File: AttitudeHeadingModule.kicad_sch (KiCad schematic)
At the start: 8 parts, among them J2 Conn_01x04, U2 ISM330DHCX, U3 MMC5983MA

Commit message: Add footprints to symbols
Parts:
- C13, C14, C17: footprint (none) -> Capacitor_SMD:C_0402_1005Metric; Listing (none) -> https://www.digikey.com/en/products/detail/samsung-electro-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
- C15: footprint (none) -> Capacitor_SMD:C_0603_1608Metric; Listing (none) -> https://www.digikey.com/en/products/detail/samsung-electro-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
- C16: footprint (none) -> Capacitor_SMD:C_1206_3216Metric; Listing (none) -> https://www.digikey.com/en/products/detail/samsung-electro-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
- J2: footprint Connector_JST_GH:GH_B04B-GH-A_1x04_P1.25mm_Vertical -> Connector_JST:JST_GH_BM04B-GHS-TBT_1x04-1MP_P1.25mm_Vertical; Listing (none) -> https://www.digikey.com/en/products/detail/jst-sales-americ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
- U2: Listing (none) -> https://www.digikey.com/en/products/detail/stmicroelectroni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
- U3: footprint MMC5983MA_MEM -> XuLab:MMC5983MA_MEM; Listing (none) -> https://www.digikey.com/en/products/detail/memsic-inc/MMC59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
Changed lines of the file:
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@@
 			)
 		)
-		(property "Footprint" "Connector_JST_GH:GH_B04B-GH-A_1x04_P1.25mm_Vertical"
+		(property "Footprint" "Connector_JST:JST_GH_BM04B-GHS-TBT_1x04-1MP_P1.25mm_Vertical"
 			(at 231.394 74.93 0)
 			(effects
@@
 			)
 		)
+		(property "Listing" "https://www.digikey.com/en/products/detail/jst-sales-america-inc/BM04B-GHS-TBT-LF-SN-N/807802"
+			(at 228.6 86.36 0)
+			(effects
+				(font
+					(size 1.27 1.27)
+				)
+				(hide yes)
+			)
+		)
 		(pin "2"
 		)
@@
 			)
 		)
-		(property "Footprint" ""
+		(property "Footprint" "Capacitor_SMD:C_0603_1608Metric"
 			(at 140.6652 123.19 0)
 			(effects
@@
 			)
 		)
-		(property "Datasheet" "~"
+		(property "Datasheet" "https://weblib.samsungsem.com/mlcc/mlcc-ec-data-sheet.do?partNumber=CL10B105KO8NNN"
 			(at 139.7 119.38 0)
 			(effects
@@
 			)
 		)
+		(property "Listing" "https://www.digikey.com/en/products/detail/samsung-electro-mechanics/CL10B105KO8NNNC/3886677"
+			(at 139.7 119.38 0)
+			(effects
+				(font
+					(size 1.27 1.27)
+				)
+				(hide yes)
+			)
+		)
 		(pin "1"
 		)
@@
 			)
 		)
-		(property "Footprint" "MMC5983MA_MEM"
+		(property "Footprint" "XuLab:MMC5983MA_MEM"
 			(at 60.96 134.874 0)
 			(effects
@@
 		)
 		(property "Description" ""
+			(at 81.28 116.84 0)
+			(effects
+				(font
+					(size 1.27 1.27)
+				)
+				(hide yes)
+			)
+		)
+		(property "Listing" "https://www.digikey.com/en/products/detail/memsic-inc/MMC5983MA/10452795"
 			(at 81.28 116.84 0)
 			(effects
@@
 			)
 		)
-		(property "Footprint" ""
+		(property "Footprint" "Capacitor_SMD:C_0402_1005Metric"
 			(at 121.6152 55.88 0)
 			(effects
@@
 			)
 		)
-		(property "Datasheet" "~"
+		(property "Datasheet" "https://mm.digikey.com/Volume0/opasdata/d220001/medias/docus/503/CL05A104KA5NNNC.pdf"
 			(at 120.65 52.07 0)
 			(effects
@@
 			)
 		)
+		(property "Listing" "https://www.digikey.com/en/products/detail/samsung-electro-mechanics/CL05A104KA5NNNC/3886701"
+			(at 120.65 52.07 0)
+			(effects
+				(font
+					(size 1.27 1.27)
+				)
+				(hide yes)
+			)
+		)
 		(pin "1"
 		)
@@
 			)
 		)
+		(property "Listing" "https://www.digikey.com/en/products/detail/stmicroelectronics/ISM330DHCXTR/10409727?s=N4IgTCBcDaIJIGUCyBmFAGAIgCQMIA0QBdAXyA"
+			(at 81.28 53.34 0)
+			(effects
+				(font
+					(size 1.27 1.27)
+				)
+				(hide yes)
+			)
+		)
 		(pin "5"
 		)
@@
 			)
 		)
-		(property "Footprint" ""
+		(property "Footprint" "Capacitor_SMD:C_0402_1005Metric"
 			(at 254.9652 92.71 0)
 			(effects
@@
 			)
 		)
-		(property "Datasheet" "~"
+		(property "Datasheet" "https://mm.digikey.com/Volume0/opasdata/d220001/medias/docus/503/CL05A104KA5NNNC.pdf"
 			(at 254 88.9 0)
 			(effects
@@
 			)
 		)
+		(property "Listing" "https://www.digikey.com/en/products/detail/samsung-electro-mechanics/CL05A104KA5NNNC/3886701"
+			(at 254 88.9 0)
+			(effects
+				(font
+					(size 1.27 1.27)
+				)
+				(hide yes)
+			)
+		)
 		(pin "1"
 		)
@@
 			)
 		)
-		(property "Footprint" ""
+		(property "Footprint" "Capacitor_SMD:C_1206_3216Metric"
 			(at 122.8852 130.81 0)
 			(effects
@@
 			)
 		)
-		(property "Datasheet" "~"
+		(property "Datasheet" "https://mm.digikey.com/Volume0/opasdata/d220001/medias/docus/658/CL31B106KAHNNNE_Spec.pdf"
 			(at 121.92 127 0)
 			(effects
@@
 			)
 		)
+		(property "Listing" "https://www.digikey.com/en/products/detail/samsung-electro-mechanics/CL31B106KAHNNNE/3887462"
+			(at 121.92 127 0)
+			(effects
+				(font
+					(size 1.27 1.27)
+				)
+				(hide yes)
+			)
+		)
 		(pin "1"
 		)
@@
 			)
 		)
-		(property "Footprint" ""
+		(property "Footprint" "Capacitor_SMD:C_0402_1005Metric"
 			(at 134.3152 55.88 0)
 			(effects
@@
 			)
 		)
-		(property "Datasheet" "~"
+		(property "Datasheet" "https://mm.digikey.com/Volume0/opasdata/d220001/medias/docus/503/CL05A104KA5NNNC.pdf"
 			(at 133.35 52.07 0)
 			(effects
@@
 			(at 133.35 52.07 0)
 			(effects
+				(font
+					(size 1.27 1.27)
+				)
+				(hide yes)
+			)
+		)
+		(property "Listing" "https://www.digikey.com/en/products/detail/samsung-electro-mechanics/CL05A104KA5NNNC/3886701"
+			(at 133.35 52.07 0)
+			(effects

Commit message: Add rest of connections
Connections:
- net +3V3 renamed +3.3V

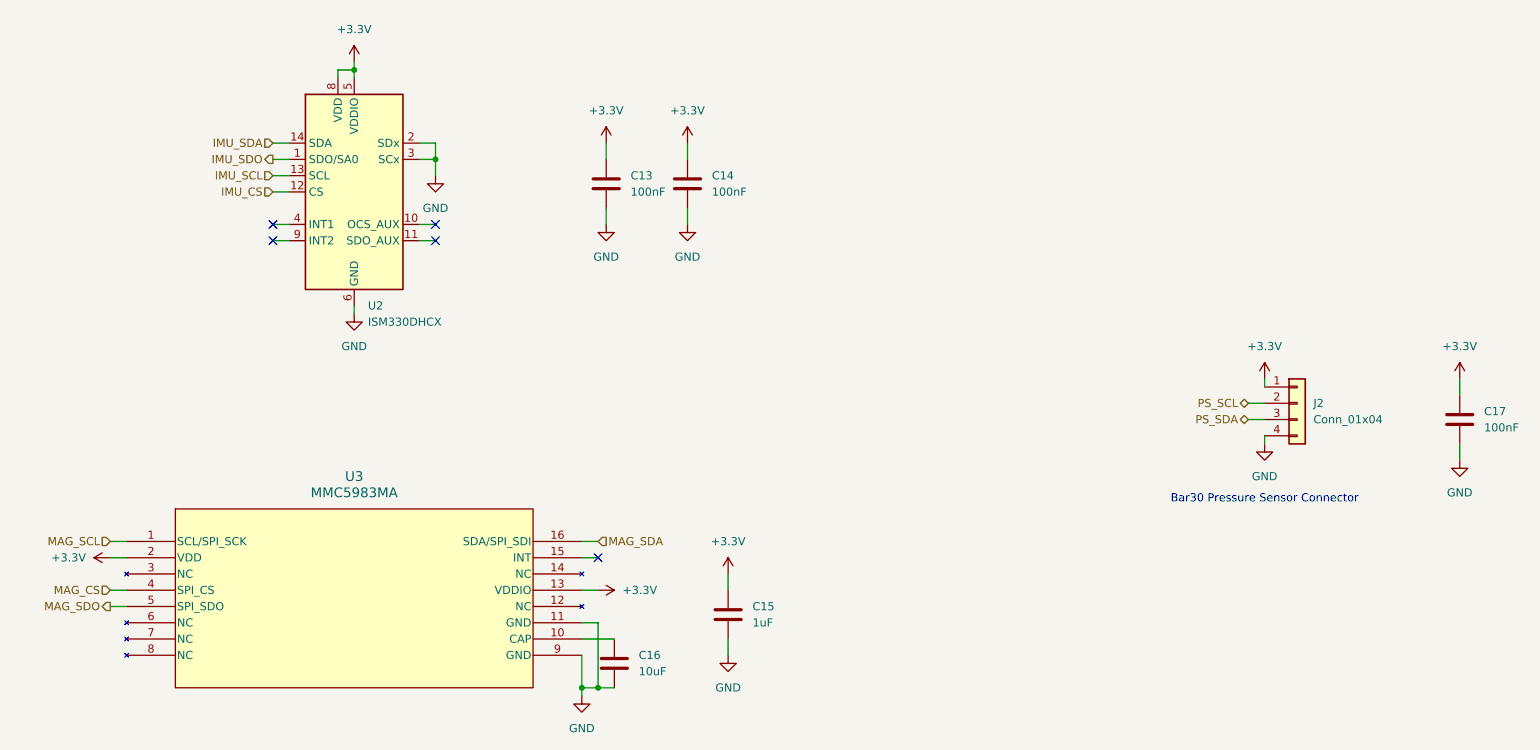
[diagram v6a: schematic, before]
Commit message: Change IMU to BMI088
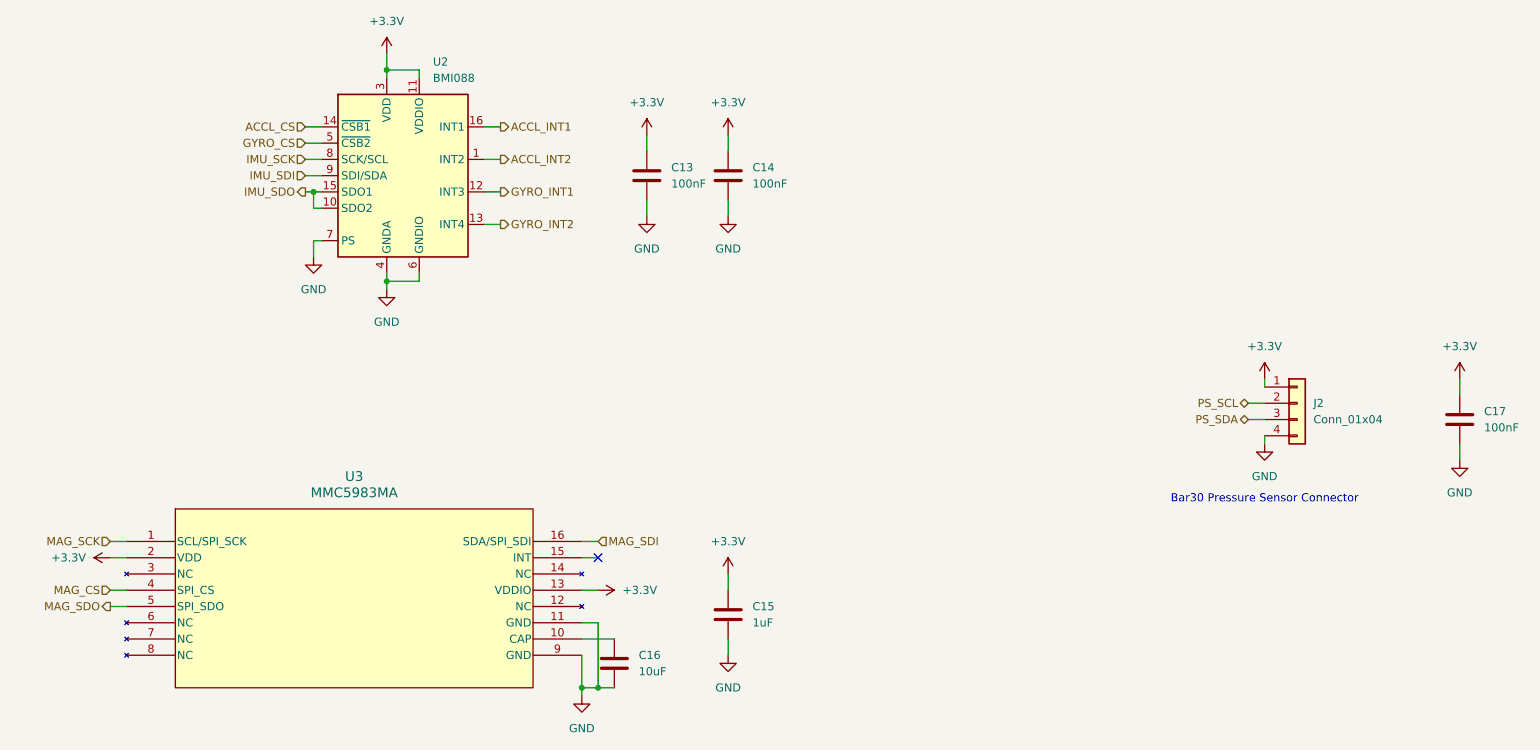
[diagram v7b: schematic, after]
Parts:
- removed U2: ISM330DHCX, Package_LGA:LGA-14_3x2.5mm_P0.5mm_LayoutBorder3x4y, symbol Sensor_Motion:ISM330DHCX
- added U2: BMI088, Package_LGA:Bosch_LGA-16_4.5x3mm_P0.5mm_LayoutBorder7x1y_ClockwisePinNumbering, symbol Sensor_Motion:BMI088
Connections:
- net +3.3V: now also U2.11 (VDDIO), U2.3 (VDD)
- net GND: now also U2.2 (GNDA), U2.4 (GNDA), U2.6 (GNDIO), U2.7 (PS)
- net IMU_SDO: now also U2.10 (SDO2), U2.15 (SDO1)
- net MAG_SCL renamed MAG_SCK
- net MAG_SDA renamed MAG_SDI
- new net ACCL_CS: U2.14 (~{CSB1})
- new net ACCL_INT1: U2.16 (INT1)
- new net ACCL_INT2: U2.1 (INT2)
- new net GYRO_CS: U2.5 (~{CSB2})
- new net GYRO_INT1: U2.12 (INT3)
- new net GYRO_INT2: U2.13 (INT4)
- new net IMU_SCK: U2.8 (SCK/SCL)
- new net IMU_SDI: U2.9 (SDI/SDA)
- no-connect marks 5 -> 1
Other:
- moved on the sheet: C13, C14

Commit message: Add interchangeable field to BOM
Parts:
- C13, C14, C15, C16, C17: Interchangeable (none) -> Yes
- J2, U2, U3: Interchangeable (none) -> No
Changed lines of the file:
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@@
+			)
+		)
+		(property "Interchangeable" "No"
+			(at 228.6 86.36 0)
+			(effects
+				(font
+					(size 1.27 1.27)
+				)
+				(hide yes)
 			)
 		)
@@
 			)
 		)
+		(property "Interchangeable" "Yes"
+			(at 139.7 119.38 0)
+			(effects
+				(font
+					(size 1.27 1.27)
+				)
+				(hide yes)
+			)
+		)
 		(pin "1"
 		)
@@
 			)
 		)
+		(property "Interchangeable" "No"
+			(at 81.28 116.84 0)
+			(effects
+				(font
+					(size 1.27 1.27)
+				)
+				(hide yes)
+			)
+		)
 		(pin "6"
 		)
@@
 			)
 		)
+		(property "Interchangeable" "Yes"
+			(at 127 50.8 0)
+			(effects
+				(font
+					(size 1.27 1.27)
+				)
+				(hide yes)
+			)
+		)
 		(pin "1"
 		)
@@
 			)
 		)
+		(property "Interchangeable" "Yes"
+			(at 254 88.9 0)
+			(effects
+				(font
+					(size 1.27 1.27)
+				)
+				(hide yes)
+			)
+		)
 		(pin "1"
 		)
@@
 			)
 		)
+		(property "Interchangeable" "Yes"
+			(at 121.92 127 0)
+			(effects
+				(font
+					(size 1.27 1.27)
+				)
+				(hide yes)
+			)
+		)
 		(pin "1"
 		)
@@
 			)
 		)
+		(property "Interchangeable" "No"
+			(at 88.9 50.8 0)
+			(effects
+				(font
+					(size 1.27 1.27)
+				)
+				(hide yes)
+			)
+		)
 		(pin "8"
 		)
@@
 			(at 139.7 50.8 0)
 			(effects
+				(font
+					(size 1.27 1.27)
+				)
+				(hide yes)
+			)
+		)
+		(property "Interchangeable" "Yes"
+			(at 139.7 50.8 0)
+			(effects
